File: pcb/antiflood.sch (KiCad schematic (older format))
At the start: 67 parts, among them J1 Barrel_Jack, J10 Screw_Terminal_01x02, J11 Screw_Terminal_01x02, J12 Screw_Terminal_01x02, J13 Screw_Terminal_01x02, J14 Screw_Terminal_01x02, J15 Screw_Terminal_01x02, J16 GS2, J2 Conn_01x04, J4 Conn_02x04_Odd_Even, J5 01x03, J7 01x03, J8 Conn_02x03_Odd_Even, J9 Conn_01x07, K1 P-5, K2 P-5, Q1 2N3904, Q2 2N3904, SW1 SW_Push, SW2 SW_Push, SW3 SW_Push, U1 ATMEGA328P-AU, U2 LM7812_TO220, U3 LM7805_TO220, U4 LM1117-3.3, Y1 16MHz

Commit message: scheme: start version 3
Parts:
- removed C3: 47, Capacitors_SMD:CP_Elec_6.3x5.7, symbol CP
- removed C5: 0.1, Capacitors_SMD:C_1206, symbol C
- removed J16: GS2, Connectors:GS2, symbol GS2
- removed J2: Conn_01x04, Socket_Strips:Socket_Strip_Straight_1x04_Pitch2.54mm, symbol Conn_01x04
- removed J8: Conn_02x03_Odd_Even, Pin_Headers:Pin_Header_Straight_2x03_Pitch2.54mm, symbol Conn_02x03_Odd_Even
- removed J9: Conn_01x07, Socket_Strips:Socket_Strip_Straight_1x07_Pitch2.54mm, symbol Conn_01x07
- removed JP1: Jumper_NC_Dual, Pin_Headers:Pin_Header_Straight_1x03_Pitch2.54mm, symbol Jumper_NC_Dual
- removed R10, R11: 33k, Resistors_SMD:R_0805, symbol R
- removed U2: LM7812_TO220, TO_SOT_Packages_THT:TO-220-3_Horizontal, symbol LM7812_TO220
- added C3: 0.1, symbol C
- added J2: Conn_02x03_Odd_Even, symbol Conn_02x03_Odd_Even
- added J3: Conn_02x05_Odd_Even, symbol Conn_02x05_Odd_Even
- added J6: Conn_01x05, symbol Conn_01x05
- added U2: MC34063, symbol MC34063
- C4, R17, R18, R19, R20, R21, R22: value 100 -> 470
- C6: value 47 -> 100
- R4: footprint Resistors_SMD:R_0805 -> (none)
- R5: value 3k3 -> 1k5; footprint Resistors_SMD:R_0805 -> (none)
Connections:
- net labels added: DBG, MISO, MOSI, PCL, PON, SCK, WCC
- net labels removed: WCE, WCR
- wire segments 238 -> 221
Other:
- note added: "TODO:\n1) replace linear stabilazier for 5VDC with DC/DC converter\n2) add control schemes for battery reserve power, use A7\n"
- moved on the sheet: C1, C10, C2, C4, C6, C7, C8, C9, J4, R1, R12, R13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

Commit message: Update scheme.
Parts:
- removed U2: MC34063, symbol MC34063
- added C?: 470p, symbol C
- added D?: D, symbol D
- added L?: 220, symbol L
- added R?: 0.33, symbol R
- added R?: 1k2, symbol R
- added R?: 3k6, symbol R
- added U?: MC34063, symbol MC34063
- C2: value 100 -> 470
- C4: value 470 -> 100
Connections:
- wire segments 221 -> 246
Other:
- moved on the sheet: C1, C10, C2, C3, C4, C6, C7, C8, C9, D2, J10, J11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

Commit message: scheme: update
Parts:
- removed J6: Conn_01x05, symbol Conn_01x05
- added C?: 470p, symbol C
- added D?: D, symbol D
- added J?: Conn_02x04_Odd_Even, symbol Conn_02x04_Odd_Even
- added L?: 220, symbol L
- added R?: 0.33, symbol R
- added R?: 1k2, symbol R
- added R?: 3k6, symbol R
- added U?: MC34063, symbol MC34063
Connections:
- wire segments 246 -> 354
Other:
- note added: "TODO:\n1) add control schemes for battery reserve power, use A7\n"
- note removed: "TODO:\n1) replace linear stabilazier for 5VDC with DC/DC converter\n2) add control schemes for battery reserve power, use A7\n"
- moved on the sheet: C8, J2, J3, R15, SW3

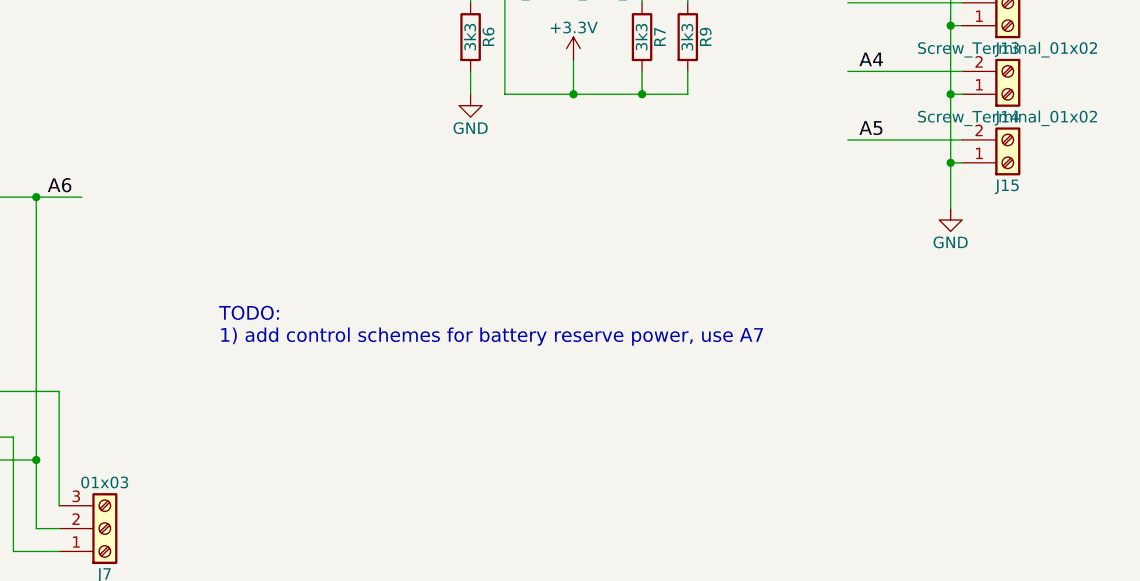
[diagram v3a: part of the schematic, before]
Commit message: Add copyright.
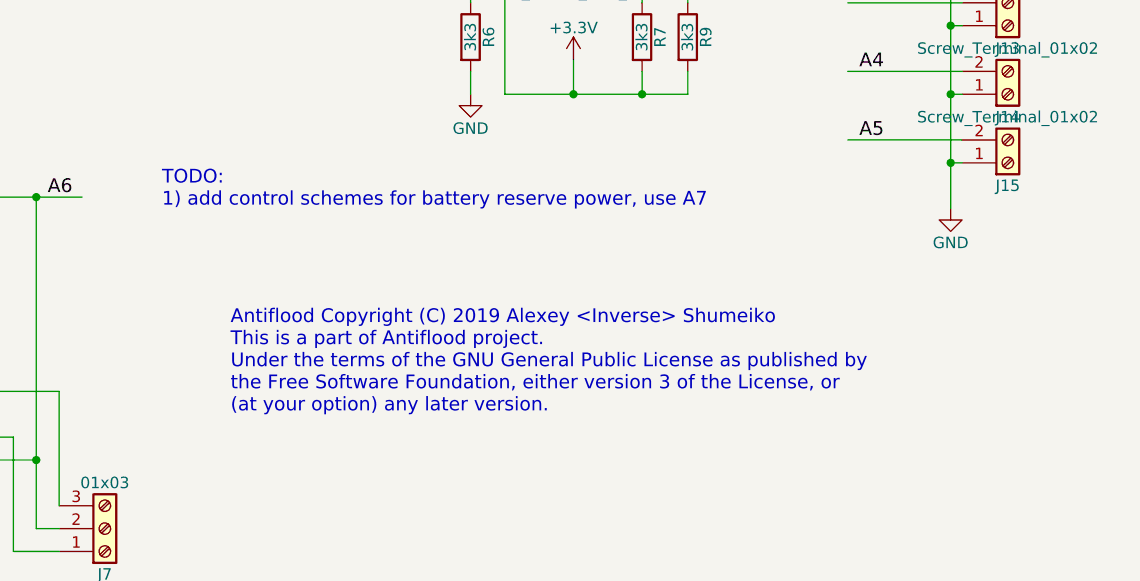
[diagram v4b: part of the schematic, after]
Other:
- note added: "Antiflood Copyright (C) 2019 Alexey <Inverse> Shumeiko\nThis is a part of Antiflood project.\nUnder the terms of the GNU General Public License as published by\nthe Free Software Foundation, either version 3 of the License, or\n(at your option) any later version.\n"
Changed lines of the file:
@@
 	1    0    0    -1
 $EndComp
-Text Notes 7000 6750 0    60   ~ 0
+Text Notes 6750 6150 0    60   ~ 0
 TODO:\n1) add control schemes for battery reserve power, use A7\n
 $Comp
@@
 	7900 1050 8050 1050
 Connection ~ 7900 1050
+Text Notes 7050 7050 0    60   ~ 0
+Antiflood Copyright (C) 2019 Alexey <Inverse> Shumeiko\nThis is a part of Antiflood project.\nUnder the terms of the GNU General Public License as published by\nthe Free Software Foundation, either version 3 of the License, or\n(at your option) any later version.\n
 $EndSCHEMATC

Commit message: Update scheme.
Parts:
- removed C?: 470p, symbol C
- removed D?: D, symbol D
- removed J?: Conn_02x04_Odd_Even, symbol Conn_02x04_Odd_Even
- removed L?: 220, symbol L
- removed R?: 0.33, symbol R
- removed R?: 1k2, symbol R
- removed R?: 3k6, symbol R
- removed U?: MC34063, symbol MC34063
- added C8: 1n5, symbol C
- added C9: 100, symbol CP
- added D3, D4: LED, symbol LED
- added D5: D, symbol D
- added J4: Conn_02x05_Odd_Even, symbol Conn_02x05_Odd_Even
- added L1: 170, symbol L
- added R10: 1k2, symbol R
- added R11: 180, symbol R
- added R13: 3k6, symbol R
- added R16, R18: R, symbol R
- added R17: 10k, symbol R
- added R5, R8: 1k, symbol R
- added R6: 0.22, symbol R
- added U5: MC34063, symbol MC34063
- added U6: TP4056, symbol TP4056
- R26: renamed from R17; value 470 -> 1k
- R27: renamed from R18; value 470 -> 1k
- R28: renamed from R19; value 470 -> 1k
- R29: renamed from R20; value 470 -> 1k
- R30: renamed from R21; value 470 -> 1k
- R31: renamed from R22; value 470 -> 1k
- gave numbers to parts that had none: 7
- renumbered C6 to C1, C8 to C10, C9 to C11, C10 to C12, C7 to C2, C2 to C3, C1 to C4, C4 to C5, C3 to C6, D6 to D10, D7 to D11, D8 to D12, D3 to D7, D4 to D8, D5 to D9, J12 to J10, J13 to J11, J14 to J12, J15 to J13, J5 to J2, J7 to J3, J4 to J5, J3 to J6, J2 to J7, J10 to J8, J11 to J9, R4 to R1, R13 to R14, R14 to R15, R3 to R19, R1 to R2, R6 to R20, R7 to R21, R8 to R22, R9 to R23, R15 to R24, R12 to R25, R5 to R3, R16 to R32, R2 to R4, U4 to U1, U1 to U2
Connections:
- net labels added: BAT, BTMP, CHG
- wire segments 354 -> 306
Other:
- note added: "TODO:\n1) add controls: A7, CHG, +12V@U5, CHRG@U6, STDBY@U6\n2) BTMP R16, R18 values"
- note removed: "TODO:\n1) add control schemes for battery reserve power, use A7\n"

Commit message: Update.
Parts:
- C6, C7, C8: footprint (none) -> Capacitors_SMD:C_1206
- C9: footprint (none) -> Capacitors_SMD:CP_Elec_6.3x5.7
- D3, D4: footprint (none) -> LEDs:LED_1206
- D5, D6: footprint (none) -> Diodes_SMD:D_SMA
- J4, J6: footprint (none) -> Socket_Strips:Socket_Strip_Straight_2x05_Pitch2.54mm
- J7: footprint (none) -> Socket_Strips:Socket_Strip_Straight_2x03_Pitch2.54mm
- L1, L2: footprint (none) -> Inductors_SMD:L_12x12mm_h6mm
- R1, R10, R11, R12, R13, R16, R17, R18, R3, R5, R6, R7, R8, R9: footprint (none) -> Resistors_SMD:R_0805
- SW1, SW2, SW3: footprint Buttons_Switches_THT:SW_Tactile_SPST_Angled_PTS645Vx83-2LFS -> Buttons_Switches_SMD:SW_SPST_SKQG
- U4, U5, U6: footprint (none) -> SMD_Packages:SOIC-8-N
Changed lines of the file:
@@
 EESchema Schematic File Version 2
-LIBS:antiflood-rescue
 LIBS:power
 LIBS:device
@@
 F 0 "SW1" H 1900 7300 50  0000 L CNN
 F 1 "SW_Push" H 1850 7140 50  0000 C CNN
-F 2 "Buttons_Switches_THT:SW_Tactile_SPST_Angled_PTS645Vx83-2LFS" H 1850 7400 50  0001 C CNN
+F 2 "Buttons_Switches_SMD:SW_SPST_SKQG" H 1850 7400 50  0001 C CNN
 F 3 "" H 1850 7400 50  0001 C CNN
 	1    1850 7200
@@
 F 0 "SW2" H 4050 7250 50  0000 L CNN
 F 1 "SW_Push" H 4000 7090 50  0000 C CNN
-F 2 "Buttons_Switches_THT:SW_Tactile_SPST_Angled_PTS645Vx83-2LFS" H 4000 7350 50  0001 C CNN
+F 2 "Buttons_Switches_SMD:SW_SPST_SKQG" H 4000 7350 50  0001 C CNN
 F 3 "" H 4000 7350 50  0001 C CNN
 	1    4000 7150
@@
 F 0 "C6" H 3525 1250 50  0000 L CNN
 F 1 "0.1" H 3525 1050 50  0000 L CNN
-F 2 "" H 3538 1000 50  0001 C CNN
+F 2 "Capacitors_SMD:C_1206" H 3538 1000 50  0001 C CNN
 F 3 "" H 3500 1150 50  0001 C CNN
 	1    3500 1150
@@
 F 0 "J6" H 8950 1350 50  0000 C CNN
 F 1 "Conn_02x05_Odd_Even" H 8950 750 50  0000 C CNN
-F 2 "" H 8900 1050 50  0001 C CNN
+F 2 "Socket_Strips:Socket_Strip_Straight_2x05_Pitch2.54mm" H 8900 1050 50  0001 C CNN
 F 3 "" H 8900 1050 50  0001 C CNN
 	1    8900 1050
@@
 F 0 "J7" H 8950 2250 50  0000 C CNN
 F 1 "Conn_02x03_Odd_Even" H 8950 1850 50  0000 C CNN
-F 2 "" H 8900 2050 50  0001 C CNN
+F 2 "Socket_Strips:Socket_Strip_Straight_2x03_Pitch2.54mm" H 8900 2050 50  0001 C CNN
 F 3 "" H 8900 2050 50  0001 C CNN
 	1    8900 2050
@@
 F 0 "SW3" H 9500 3750 50  0000 L CNN
 F 1 "SW_Push" H 9450 3590 50  0000 C CNN
-F 2 "Buttons_Switches_THT:SW_Tactile_SPST_Angled_PTS645Vx83-2LFS" H 9450 3850 50  0001 C CNN
+F 2 "Buttons_Switches_SMD:SW_SPST_SKQG" H 9450 3850 50  0001 C CNN
 F 3 "" H 9450 3850 50  0001 C CNN
 	1    9450 3650
@@
 F 0 "R3" V 3230 6850 50  0000 C CNN
 F 1 "1k5" V 3150 6850 50  0000 C CNN
-F 2 "" V 3080 6850 50  0001 C CNN
+F 2 "Resistors_SMD:R_0805" V 3080 6850 50  0001 C CNN
 F 3 "" H 3150 6850 50  0001 C CNN
 	1    3150 6850
@@
 F 0 "R1" V 1080 6900 50  0000 C CNN
 F 1 "1k5" V 1000 6900 50  0000 C CNN
-F 2 "" V 930 6900 50  0001 C CNN
+F 2 "Resistors_SMD:R_0805" V 930 6900 50  0001 C CNN
 F 3 "" H 1000 6900 50  0001 C CNN
 	1    1000 6900
@@
 F 0 "U4" H 4950 1450 60  0000 L CNN
 F 1 "MC34063" H 4950 850 60  0000 L CNN
-F 2 "" H 5150 1100 60  0000 C CNN
+F 2 "SMD_Packages:SOIC-8-N" H 5150 1100 60  0001 C CNN
 F 3 "" H 5150 1100 60  0000 C CNN
 	1    5250 1100
@@
 F 0 "R7" V 4430 850 50  0000 C CNN
 F 1 "0.33" V 4350 850 50  0000 C CNN
-F 2 "" V 4280 850 50  0001 C CNN
+F 2 "Resistors_SMD:R_0805" V 4280 850 50  0001 C CNN
 F 3 "" H 4350 850 50  0001 C CNN
 	1    4350 850
@@
 F 0 "R9" V 4480 1500 50  0000 C CNN
 F 1 "1k2" V 4400 1500 50  0000 C CNN
-F 2 "" V 4330 1500 50  0001 C CNN
+F 2 "Resistors_SMD:R_0805" V 4330 1500 50  0001 C CNN
 F 3 "" H 4400 1500 50  0001 C CNN
 	1    4400 1500
@@
 F 0 "R12" V 4980 1500 50  0000 C CNN
 F 1 "3k6" V 4900 1500 50  0000 C CNN
-F 2 "" V 4830 1500 50  0001 C CNN
+F 2 "Resistors_SMD:R_0805" V 4830 1500 50  0001 C CNN
 F 3 "" H 4900 1500 50  0001 C CNN
 	1    4900 1500
@@
 F 0 "C7" H 6025 1450 50  0000 L CNN
 F 1 "470p" H 6025 1250 50  0000 L CNN
-F 2 "" H 6038 1200 50  0001 C CNN
+F 2 "Capacitors_SMD:C_1206" H 6038 1200 50  0001 C CNN
 F 3 "" H 6000 1350 50  0001 C CNN
 	1    6000 1350
@@
 F 0 "L2" V 6100 800 50  0000 C CNN
 F 1 "220" V 6225 800 50  0000 C CNN
-F 2 "" H 6150 800 50  0001 C CNN
+F 2 "Inductors_SMD:L_12x12mm_h6mm" H 6150 800 50  0001 C CNN
 F 3 "" H 6150 800 50  0001 C CNN
 	1    6150 800
@@
 F 0 "D6" H 6350 1450 50  0000 C CNN
 F 1 "D" H 6350 1250 50  0000 C CNN
-F 2 "" H 6350 1350 50  0001 C CNN
+F 2 "Diodes_SMD:D_SMA" H 6350 1350 50  0001 C CNN
 F 3 "" H 6350 1350 50  0001 C CNN
 	1    6350 1350
@@
 F 0 "D4" H 4850 3000 50  0000 C CNN
 F 1 "LED" H 4850 2800 50  0000 C CNN
-F 2 "" H 4850 2900 50  0001 C CNN
+F 2 "LEDs:LED_1206" H 4850 2900 50  0001 C CNN
 F 3 "" H 4850 2900 50  0001 C CNN
 	1    4850 2900
@@
 F 0 "D3" H 4500 3100 50  0000 C CNN
 F 1 "LED" H 4500 2900 50  0000 C CNN
-F 2 "" H 4500 3000 50  0001 C CNN
+F 2 "LEDs:LED_1206" H 4500 3000 50  0001 C CNN
 F 3 "" H 4500 3000 50  0001 C CNN
 	1    4500 3000
@@
 F 0 "R8" V 4430 2650 50  0000 C CNN
 F 1 "1k" V 4350 2650 50  0000 C CNN
-F 2 "" V 4280 2650 50  0001 C CNN
+F 2 "Resistors_SMD:R_0805" V 4280 2650 50  0001 C CNN
 F 3 "" H 4350 2650 50  0001 C CNN
 	1    4350 2650
@@
 F 0 "R5" V 4230 2650 50  0000 C CNN
 F 1 "1k" V 4150 2650 50  0000 C CNN
-F 2 "" V 4080 2650 50  0001 C CNN
+F 2 "Resistors_SMD:R_0805" V 4080 2650 50  0001 C CNN
 F 3 "" H 4150 2650 50  0001 C CNN
 	1    4150 2650
@@
 F 0 "R17" V 6280 3250 50  0000 C CNN
 F 1 "10k" V 6200 3250 50  0000 C CNN
-F 2 "" V 6130 3250 50  0001 C CNN
+F 2 "Resistors_SMD:R_0805" V 6130 3250 50  0001 C CNN
 F 3 "" H 6200 3250 50  0001 C CNN
 	1    6200 3250
@@
 F 0 "J4" H 7500 1350 50  0000 C CNN
 F 1 "Conn_02x05_Odd_Even" H 7500 750 50  0000 C CNN
-F 2 "" H 7450 1050 50  0001 C CNN
+F 2 "Socket_Strips:Socket_Strip_Straight_2x05_Pitch2.54mm" H 7450 1050 50  0001 C CNN
 F 3 "" H 7450 1050 50  0001 C CNN
 	1    7450 1050
@@
 F 0 "R18" V 6480 3250 50  0000 C CNN
 F 1 "R" V 6400 3250 50  0000 C CNN
-F 2 "" V 6330 3250 50  0001 C CNN
+F 2 "Resistors_SMD:R_0805" V 6330 3250 50  0001 C CNN
 F 3 "" H 6400 3250 50  0001 C CNN
 	1    6400 3250
@@
 F 0 "R16" V 6230 2400 50  0000 C CNN
 F 1 "R" V 6150 2400 50  0000 C CNN
-F 2 "" V 6080 2400 50  0001 C CNN
+F 2 "Resistors_SMD:R_0805" V 6080 2400 50  0001 C CNN
 F 3 "" H 6150 2400 50  0001 C CNN
 	1    6150 2400
@@
 F 0 "C9" H 6675 3350 50  0000 L CNN
 F 1 "100" H 6675 3150 50  0000 L CNN
-F 2 "" H 6688 3100 50  0001 C CNN
+F 2 "Capacitors_SMD:CP_Elec_6.3x5.7" H 6688 3100 50  0001 C CNN
 F 3 "" H 6650 3250 50  0001 C CNN
 	1    6650 3250
@@
 F 0 "U5" H 5000 4900 60  0000 L CNN
 F 1 "MC34063" H 5000 4300 60  0000 L CNN
-F 2 "" H 5200 4550 60  0000 C CNN
+F 2 "SMD_Packages:SOIC-8-N" H 5200 4550 60  0001 C CNN
 F 3 "" H 5200 4550 60  0000 C CNN
 	1    5300 4550
@@
 F 0 "R10" V 4530 4950 50  0000 C CNN
 F 1 "1k2" V 4450 4950 50  0000 C CNN
-F 2 "" V 4380 4950 50  0001 C CNN
+F 2 "Resistors_SMD:R_0805" V 4380 4950 50  0001 C CNN
 F 3 "" H 4450 4950 50  0001 C CNN
 	1    4450 4950
@@
 F 0 "R13" V 5030 4950 50  0000 C CNN
 F 1 "3k6" V 4950 4950 50  0000 C CNN
-F 2 "" V 4880 4950 50  0001 C CNN
+F 2 "Resistors_SMD:R_0805" V 4880 4950 50  0001 C CNN
 F 3 "" H 4950 4950 50  0001 C CNN
 	1    4950 4950
@@
 F 0 "C8" H 6125 4900 50  0000 L CNN
 F 1 "1n5" H 6125 4700 50  0000 L CNN
-F 2 "" H 6138 4650 50  0001 C CNN
+F 2 "Capacitors_SMD:C_1206" H 6138 4650 50  0001 C CNN
 F 3 "" H 6100 4800 50  0001 C CNN
 	1    6100 4800
@@
 F 0 "L1" V 5300 4100 50  0000 C CNN
 F 1 "170" V 5425 4100 50  0000 C CNN
-F 2 "" H 5350 4100 50  0001 C CNN
+F 2 "Inductors_SMD:L_12x12mm_h6mm" H 5350 4100 50  0001 C CNN
 F 3 "" H 5350 4100 50  0001 C CNN
 	1    5350 4100
@@
 F 0 "D5" H 6200 4450 50  0000 C CNN
 F 1 "D" H 6200 4250 50  0000 C CNN
-F 2 "" H 6200 4350 50  0001 C CNN
+F 2 "Diodes_SMD:D_SMA" H 6200 4350 50  0001 C CNN
 F 3 "" H 6200 4350 50  0001 C CNN
 	1    6200 4350
@@
 F 0 "U6" H 5250 3250 60  0000 L CNN
 F 1 "TP4056" H 5950 3250 60  0000 R CNN
-F 2 "" H 5600 2850 60  0000 C CNN
+F 2 "SMD_Packages:SOIC-8-N" H 5600 2850 60  0001 C CNN
 F 3 "" H 5600 2850 60  0000 C CNN
 	1    5600 2850
@@
 F 0 "R11" V 4680 4100 50  0000 C CNN
 F 1 "180" V 4600 4100 50  0000 C CNN
-F 2 "" V 4530 4100 50  0001 C CNN
+F 2 "Resistors_SMD:R_0805" V 4530 4100 50  0001 C CNN
 F 3 "" H 4600 4100 50  0001 C CNN
 	1    4600 4100
@@
 F 0 "R6" V 4280 4100 50  0000 C CNN
 F 1 "0.22" V 4200 4100 50  0000 C CNN
-F 2 "" V 4130 4100 50  0001 C CNN
+F 2 "Resistors_SMD:R_0805" V 4130 4100 50  0001 C CNN
 F 3 "" H 4200 4100 50  0001 C CNN
 	1    4200 4100
